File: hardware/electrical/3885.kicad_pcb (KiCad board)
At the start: 4 copper layers, 33 x 77 mm, 112 parts, among them J1 USB_B_Micro, J2 TC2030, J3 Micro_SD_Card_Det1, J4 JST-PH, J5 FFC, Q1 AO3400A, Q2 AO3400A, Q3 AO3401A, Q4 AO3401A, Q5 2N7002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

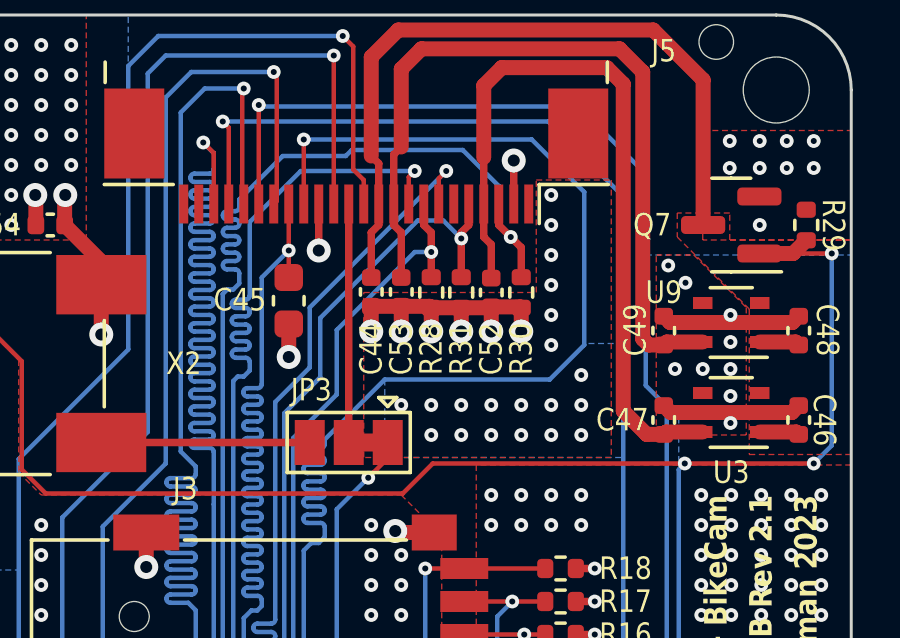
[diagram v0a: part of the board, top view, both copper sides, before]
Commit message: SCL and SDA pulled-up not pulled-down
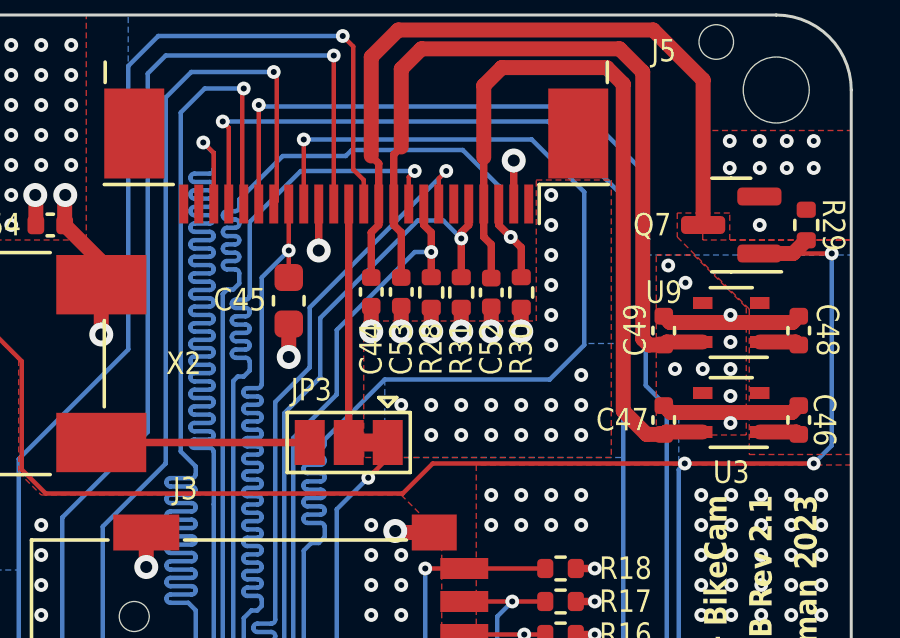
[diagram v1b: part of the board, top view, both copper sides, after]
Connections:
- R30 pad 1: GND -> VDD
- R31 pad 1: GND -> VDD
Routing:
- net GND: track 116.0 -> 109.4 mm, vias 434 -> 432
- net VDD: track 63.9 -> 65.5 mm, vias 52 -> 54

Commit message: Fix STAT LED drive circuit
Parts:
- added R4: 10k, Resistor_SMD:R_0402_1005Metric, F.Cu at (153.7, 139.9)
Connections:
- Q8 pad 2: Net-(Q8-S) -> GND
- Q8 pad 3: GND -> Net-(Q8-D)
- R11 pad 2: Net-(Q8-S) -> Net-(Q8-D)
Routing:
- net Net-(Q8-D): track 0.00 -> 2.94 mm
- net Net-(Q8-S): track 2.19 -> 0.00 mm
- net Net-(Q8-G): track 3.63 -> 5.25 mm
- net GND: track 109.4 -> 108.3 mm, vias 432 -> 431

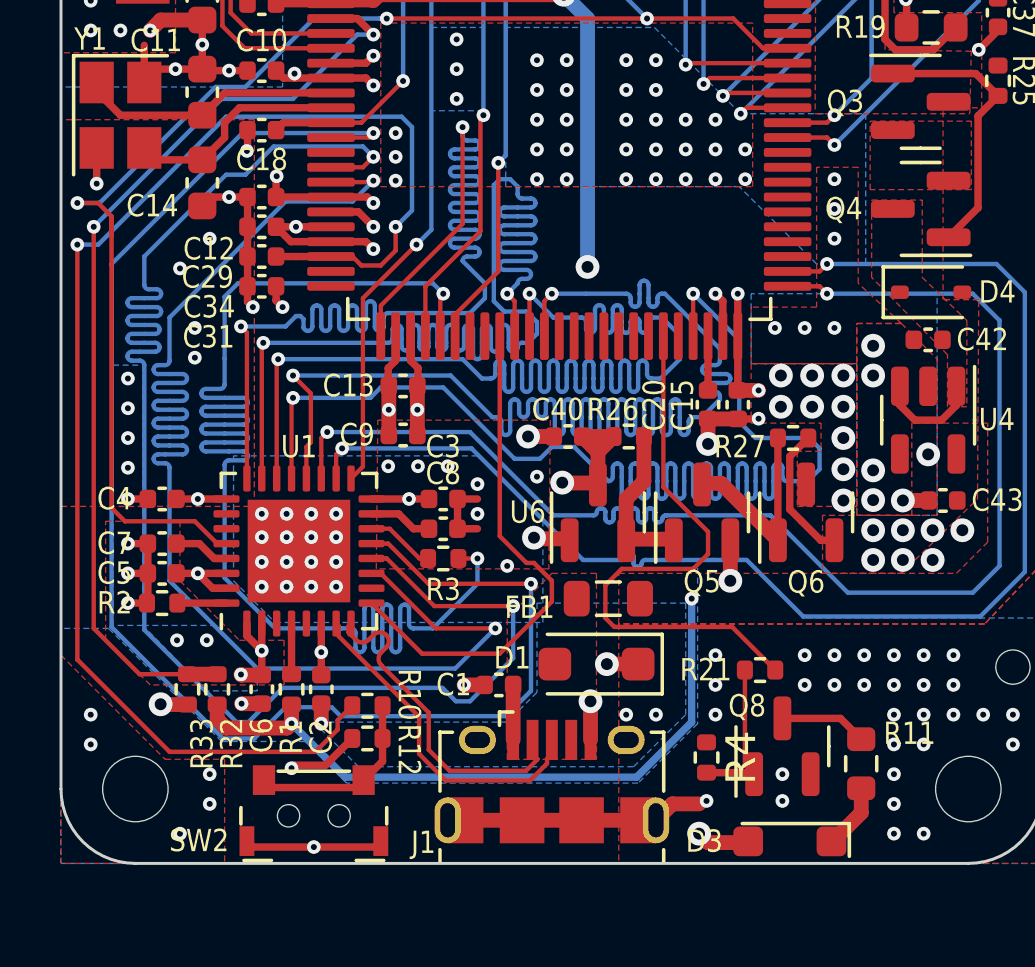
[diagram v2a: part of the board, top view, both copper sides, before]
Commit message: Replace USB connector with SMD part
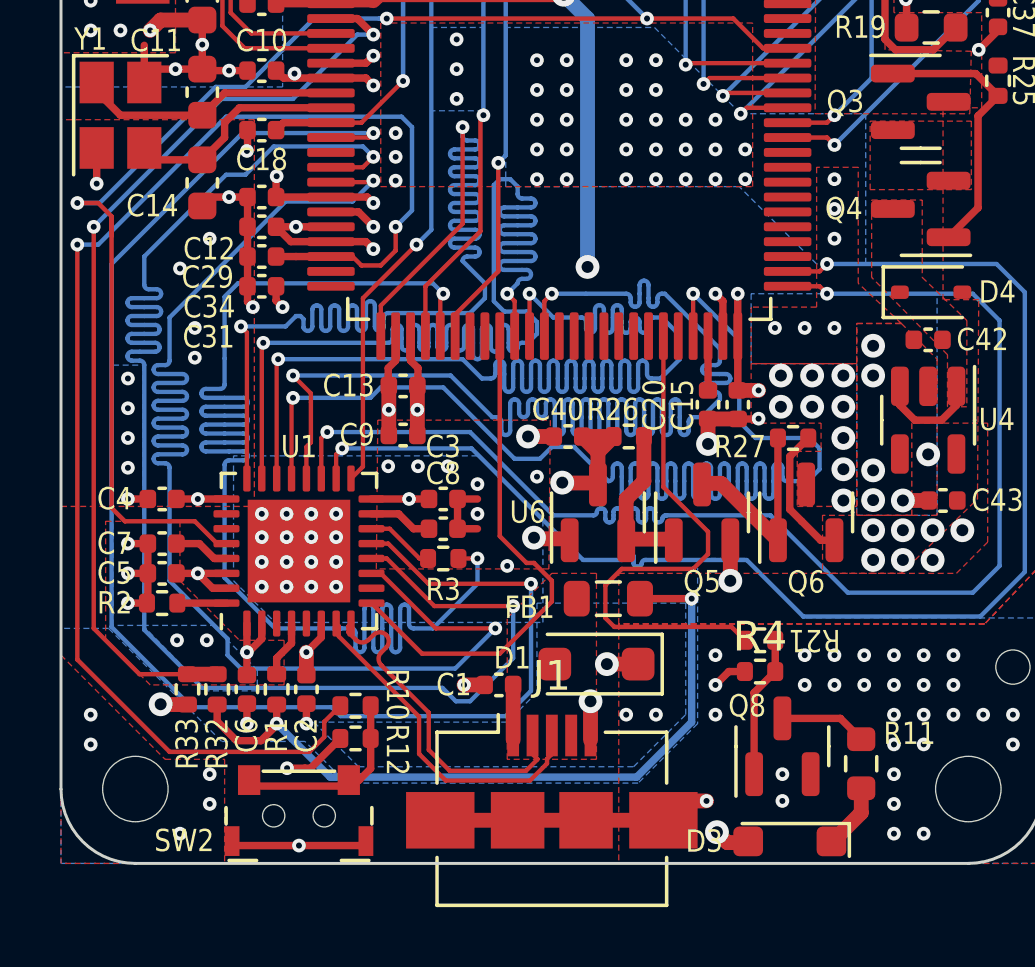
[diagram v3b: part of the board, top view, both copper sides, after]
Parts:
- J1: footprint Connector_USB:USB_Micro-B_Amphenol_10118194_Horizontal -> Connector_USB:USB_Micro-B_Amphenol_10104110_Horizontal
- moved R4 3.40 mm to (155.5, 137.1), turned to 0 degrees
- moved R21 1.00 mm to (155.5, 136.0), turned to 0 degrees
- moved C2 0.50 mm to (140.2, 137.7)
- moved C6 0.50 mm to (138.2, 137.7)
- moved R1 0.50 mm to (139.2, 137.7)
- moved SW2 0.50 mm to (140.0, 141.9)
- moved R10 0.40 mm to (141.9, 138.2)
- moved R12 0.40 mm to (141.9, 139.3)
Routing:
- net VBUS: track 22.9 -> 25.1 mm
- net STAT: track 19.4 -> 17.9 mm
- net GND: track 108.3 -> 109.5 mm, vias 431 -> 430
- net USB_OTG_HS_ULPI_DIR: track 53.2 -> 52.3 mm
- net USB_OTG_HS_ULPI_STP: track 50.4 -> 49.5 mm
- net Net-(R10-Pad2): track 6.02 -> 6.53 mm

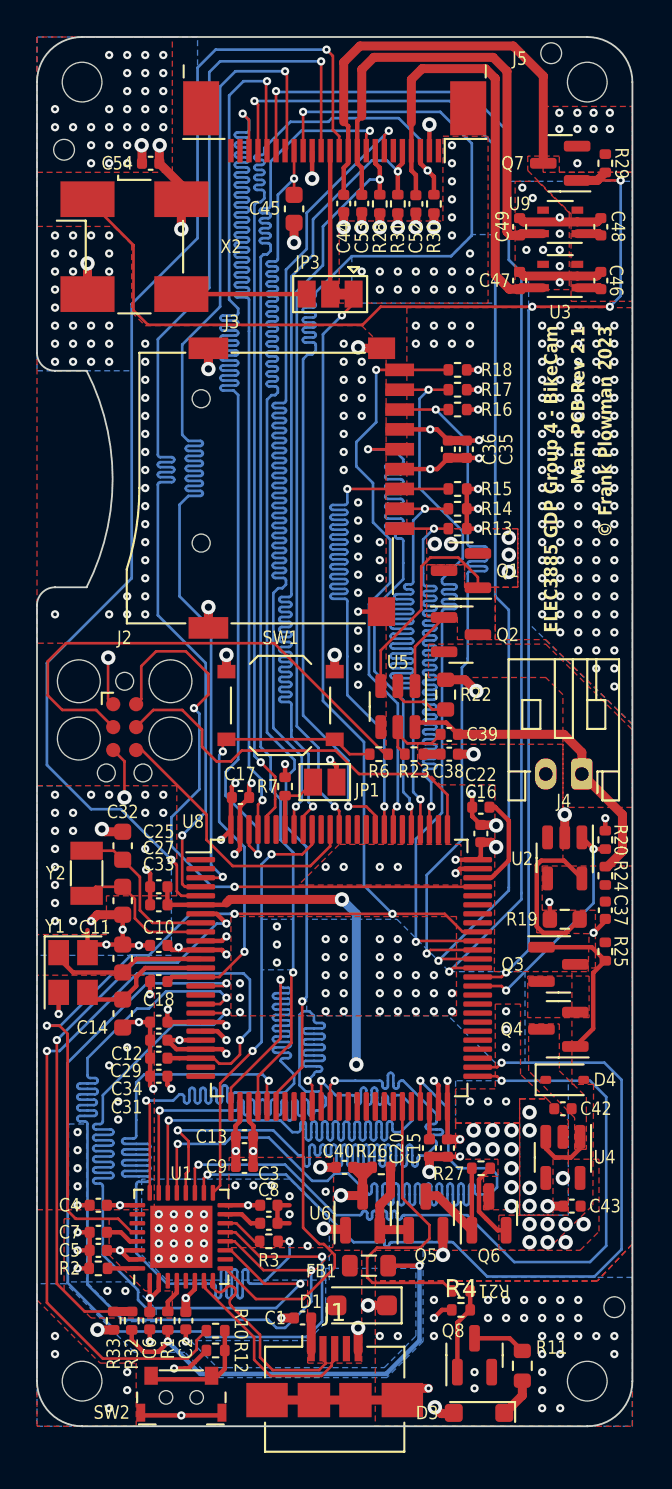
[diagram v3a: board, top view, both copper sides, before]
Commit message: Add J6 to directly power with 3.3V
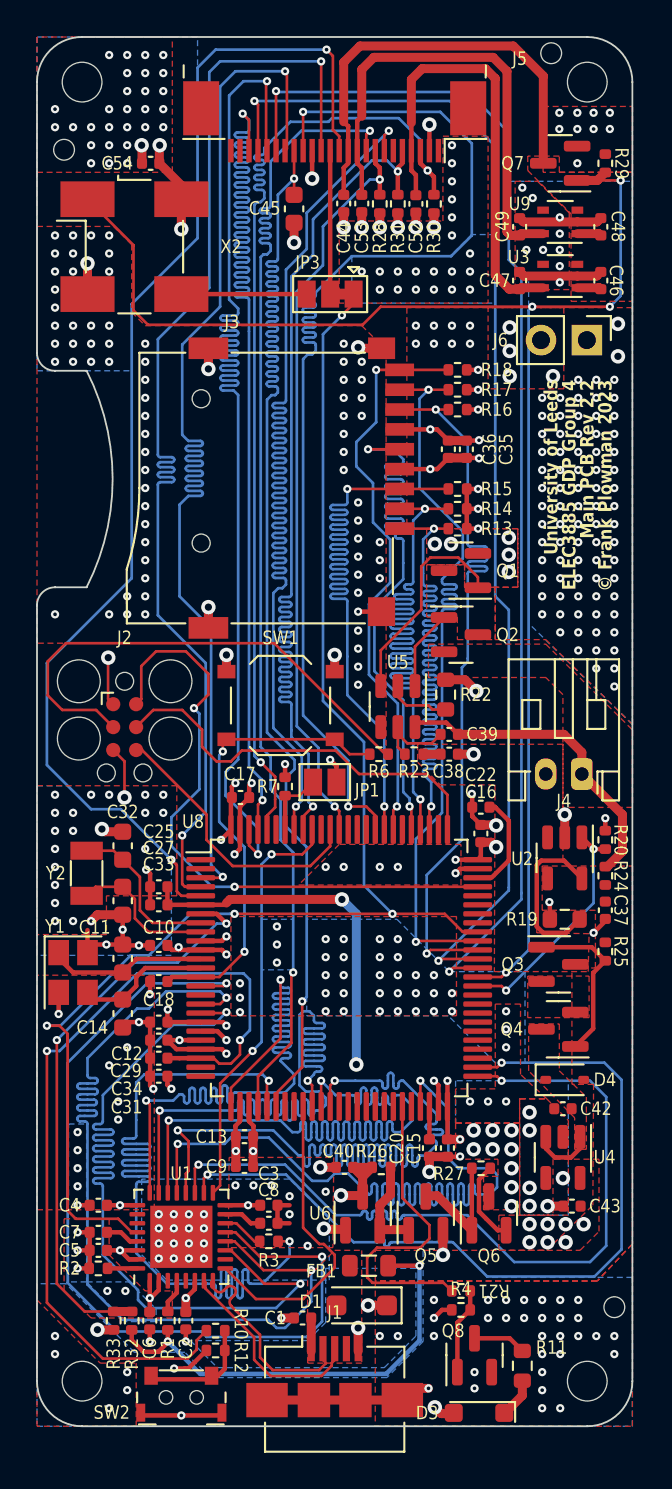
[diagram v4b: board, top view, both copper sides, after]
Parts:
- added J6: 2.54mm, Connector_PinHeader_2.54mm:PinHeader_1x02_P2.54mm_Vertical, F.Cu at (162.5, 83.3)
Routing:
- net VDD: vias 54 -> 64
- net GND: vias 430 -> 409
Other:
- board text added: "ELEC3885 GDP Group 4"
- board text added: "Main PCB Rev 2.2"
- board text added: "University of Leeds"
- board text removed: "ELEC3885 GDP Group 4 - BikeCam"
- board text removed: "Main PCB Rev 2.1"

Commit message: Fix power button footprint
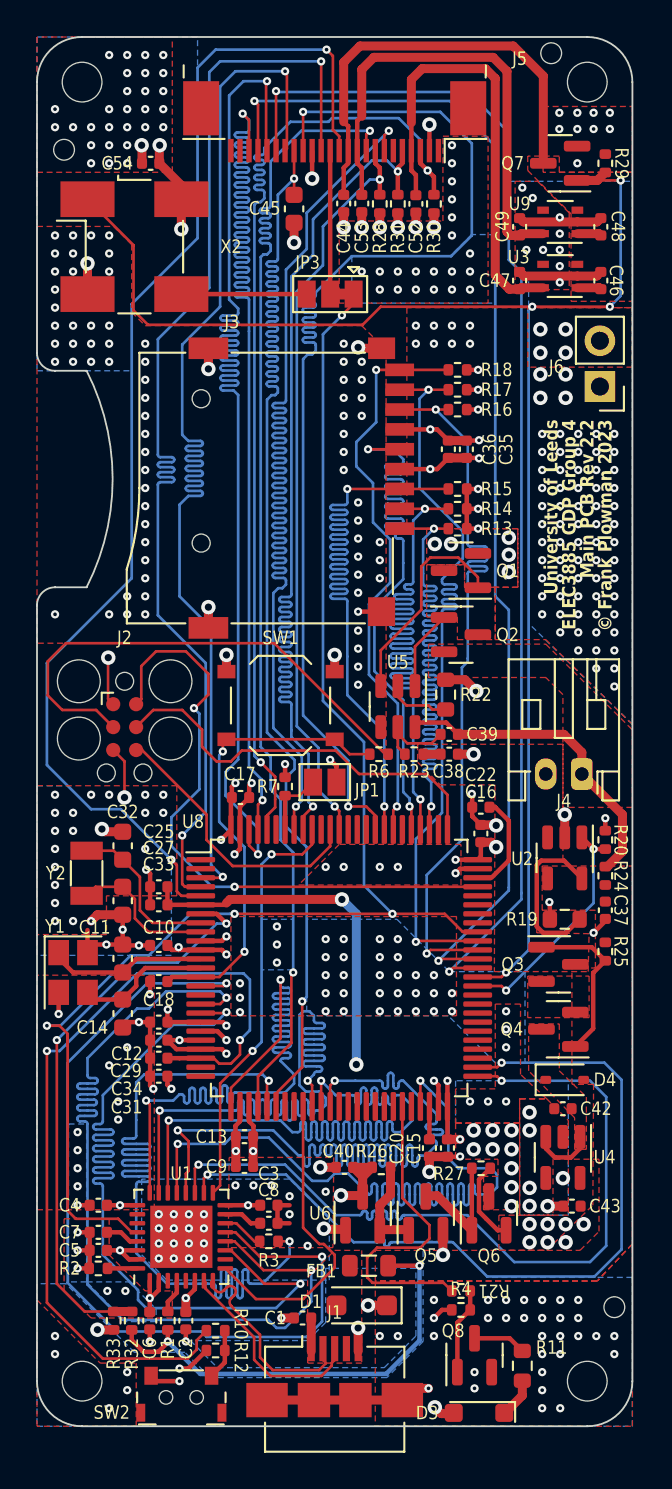
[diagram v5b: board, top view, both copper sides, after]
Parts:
- moved J6 2.68 mm to (163.2, 85.9), turned to 180 degrees
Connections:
- SW2 pad 1: VDD -> Net-(R10-Pad2)
- SW2 pad 2: Net-(R10-Pad2) -> VDD
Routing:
- net Net-(R10-Pad2): track 6.53 -> 2.80 mm
- net VDD: track 65.1 -> 62.4 mm, vias 64 -> 58
- net GND: track 109.5 -> 109.2 mm, vias 409 -> 404

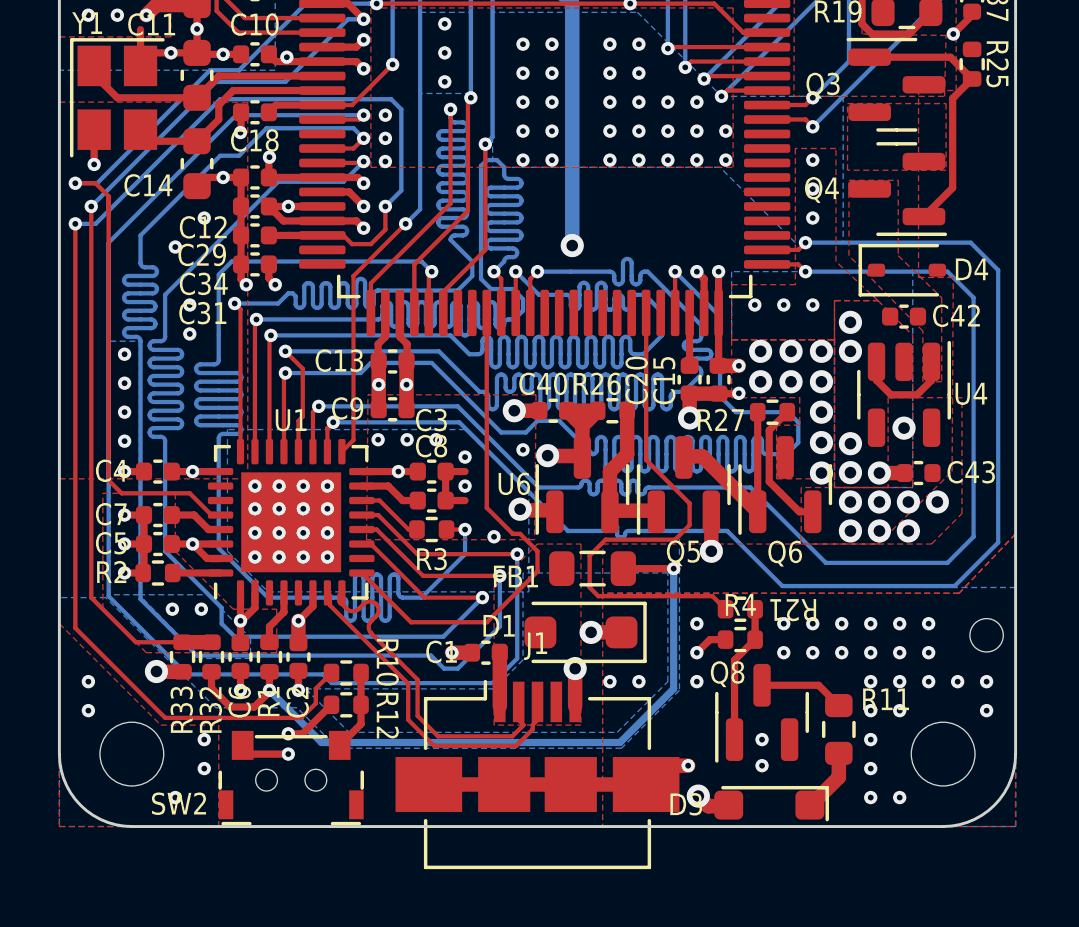
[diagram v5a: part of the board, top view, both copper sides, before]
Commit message: Add capacitor to voltage supervisor circuit
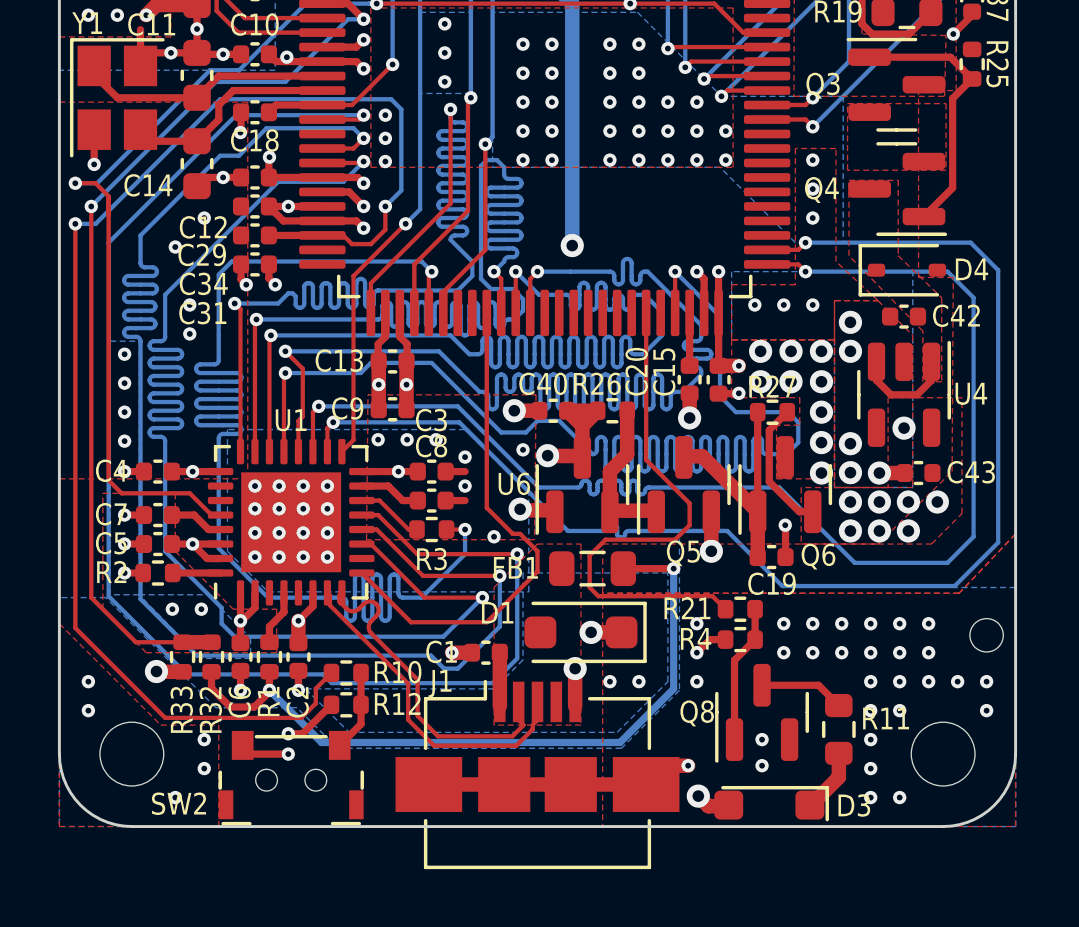
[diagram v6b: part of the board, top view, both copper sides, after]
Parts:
- added C19: 100n, Capacitor_SMD:C_0402_1005Metric, F.Cu at (156.6, 134.2)
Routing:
- net GND: track 109.2 -> 103.3 mm, vias 404 -> 405
- net Net-(Q5-D): track 6.78 -> 8.34 mm
